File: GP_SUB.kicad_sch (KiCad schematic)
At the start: 35 parts, among them J13 Conn_01x10, J14 Conn_01x10, J32 Conn_01x02, J5 Conn_02x10_Odd_Even, U1 TPS76333, U2 TXB0104RUT, U5 TXB0104RUT

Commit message: Rails alim + libs
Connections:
- net SD_MOS renamed SDMOS
- net VBUS renamed P5VAN

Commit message: Ready for review
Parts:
- removed R13, R14, R15, R16, R17, R18, R19, R20: 0R, Resistor_SMD:R_0201_0603Metric, symbol Device:R_Small
- removed R40, R42, R43, R45, R46, R48, R49, R51: 0R, Resistor_SMD:R_0603_1608Metric, symbol Device:R_Small
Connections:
- net P11 is gone; now on net TP7_Pin11: J13.7 (Pin_7), J5.13 (Pin_13)
- net P12 is gone; now on net TP15_Pin12: J14.6 (Pin_6), J5.5 (Pin_5)
- net P13 is gone; now on net TP8_Pin13: J13.8 (Pin_8), J5.14 (Pin_14)
- net P14: now also U2.2 (A1)
- net P16: now also U2.3 (A2)
- net P7: now also U2.5 (A4)
- net P8: now also U5.5 (A4)
- net P9: now also U5.3 (A2)
- net TP15_Pin12: no longer U2.8 (B3)
- net TP7_Pin11: no longer U5.10 (B1)
- net TP8_Pin13: no longer U5.8 (B3)
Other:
- note removed: "Bypass LevelShifter"

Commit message: For review
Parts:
- R8: value 1k -> 4k7
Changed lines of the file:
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@@
 			)
 		)
-		(property "Value" "1k"
+		(property "Value" "4k7"
 			(at 139.319 37.973 0)
 			(show_name no)

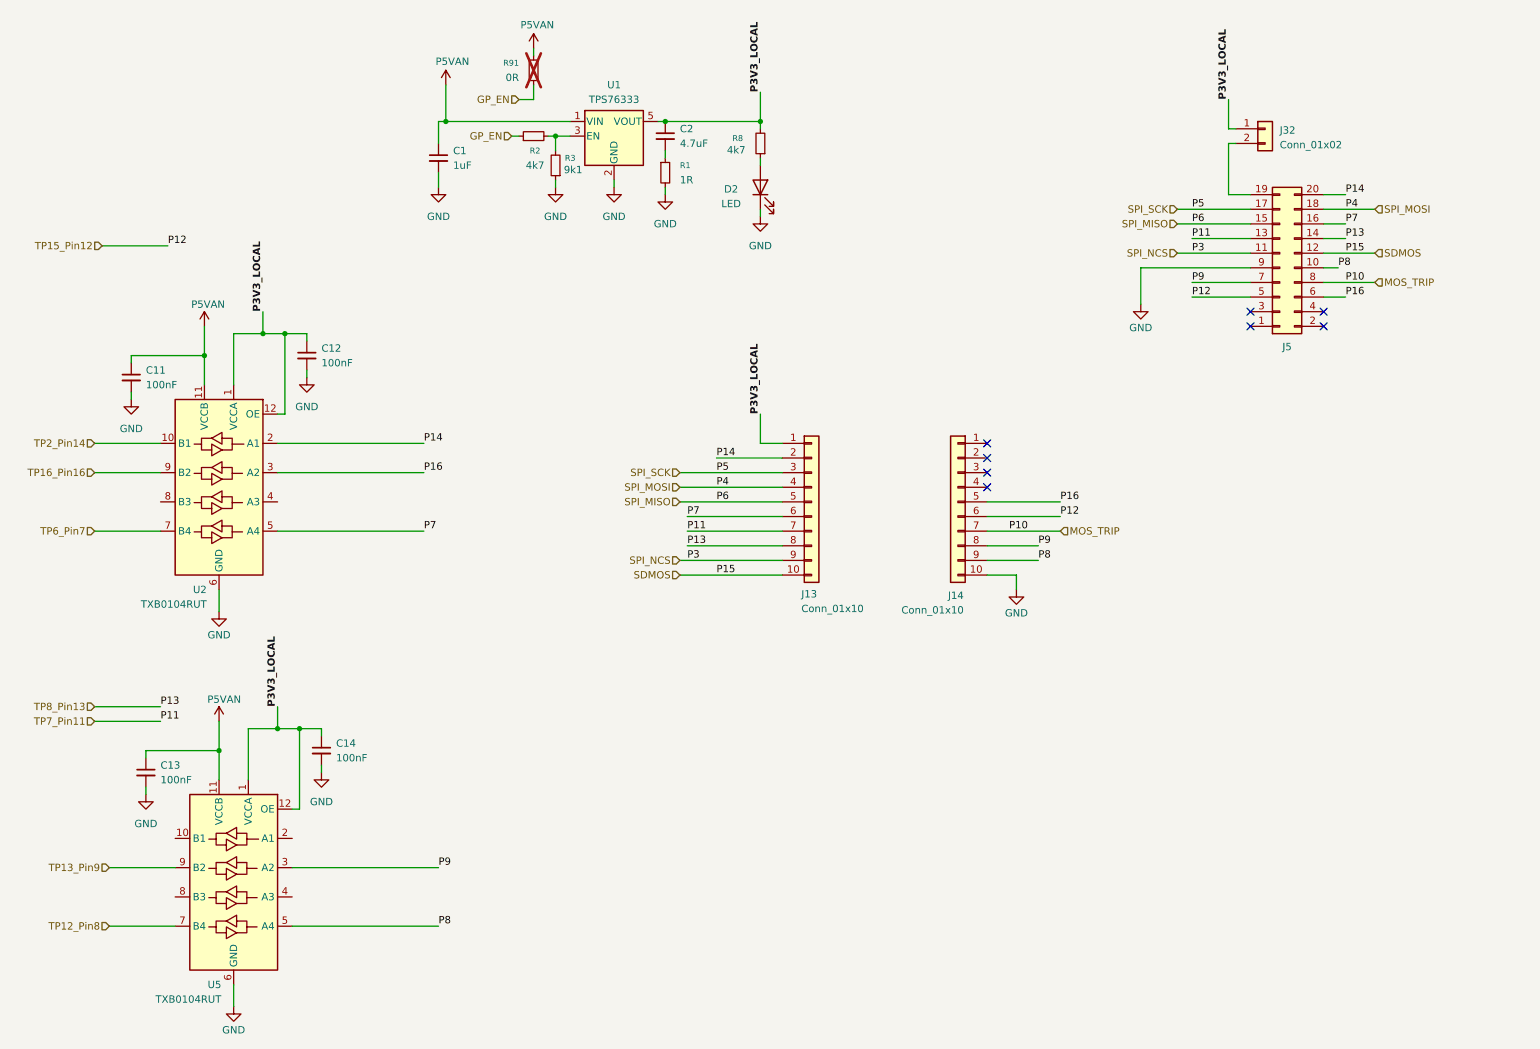
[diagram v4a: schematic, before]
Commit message: Refactor GreenPak Pinout
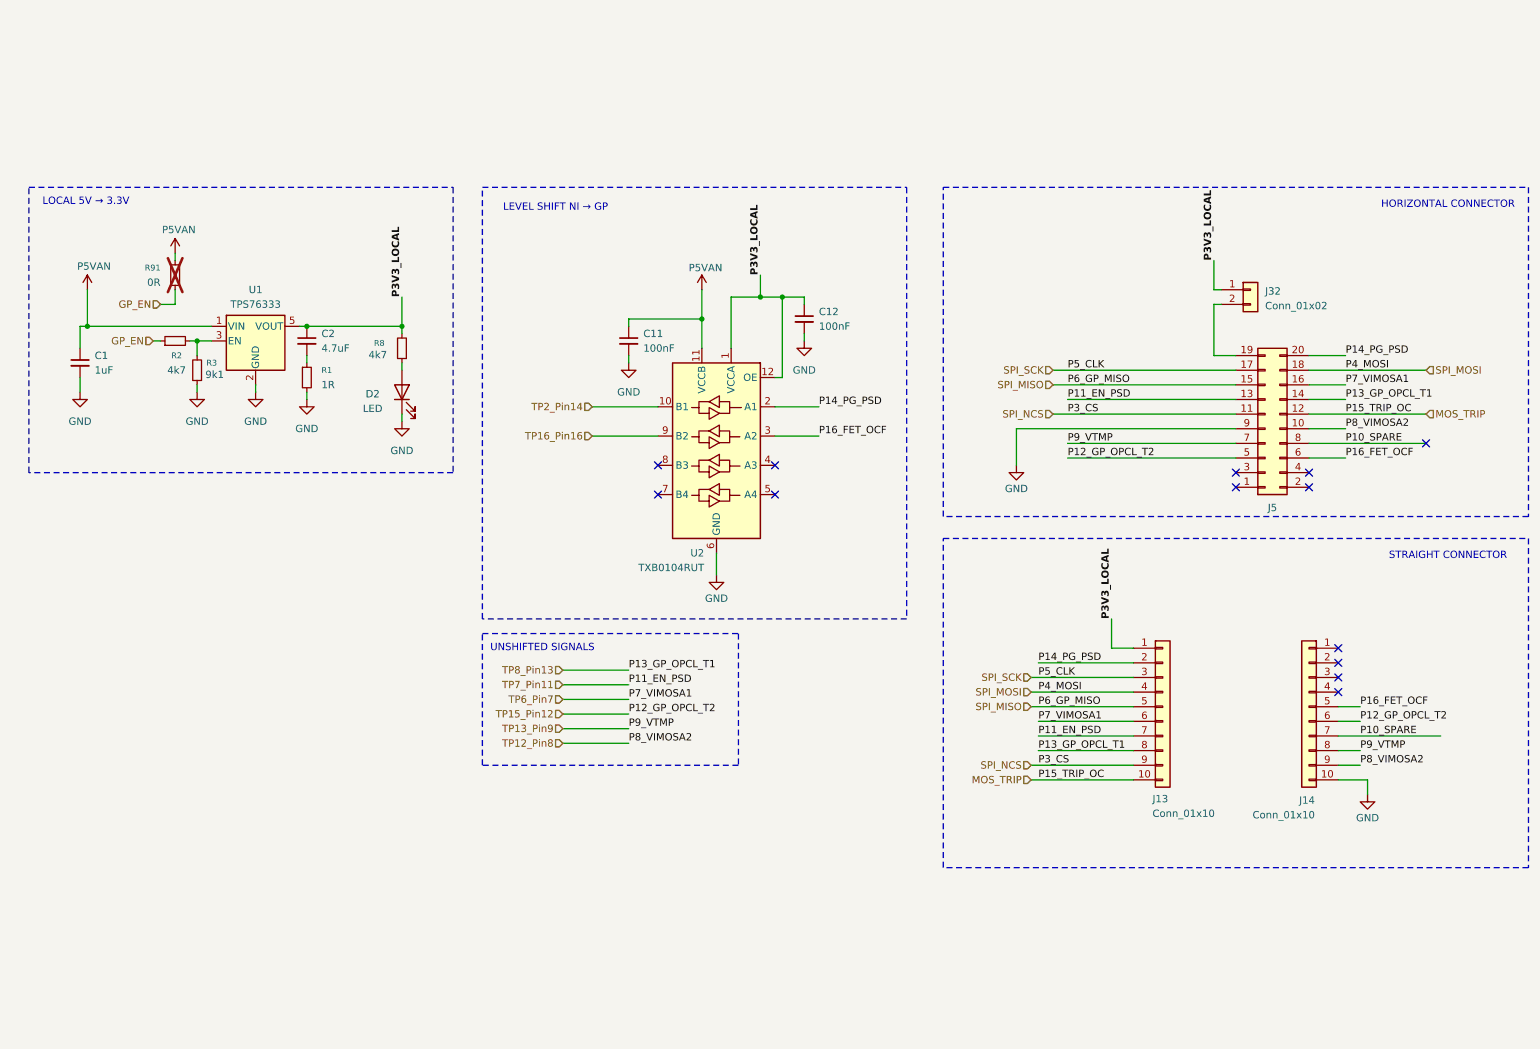
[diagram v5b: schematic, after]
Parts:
- removed C13, C14: 100nF, Capacitor_SMD:C_0402_1005Metric, symbol Device:C_Small
- removed U5: TXB0104RUT, Package_DFN_QFN:Texas_R-PUQFN-N12, symbol Logic_LevelTranslator:TXB0104RUT
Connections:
- net P8 is gone; now on net TP12_Pin8: J14.9 (Pin_9), J5.10 (Pin_10)
- net P9 is gone; now on net TP13_Pin9: J14.8 (Pin_8), J5.7 (Pin_7)
- net SDMOS is gone; now on net MOS_TRIP: J13.10 (Pin_10), J5.12 (Pin_12)
- net MOS_TRIP: no longer J14.7 (Pin_7), J5.8 (Pin_8)
- net TP6_Pin7: now also J13.6 (Pin_6), J5.16 (Pin_16); no longer U2.7 (B4)
- net P14 renamed P14_PG_PSD
- net P16 renamed P16_FET_OCF
- removed net P7: J13.6 (Pin_6), J5.16 (Pin_16), U2.5 (A4)
- new net P10_SPARE: J14.7 (Pin_7), J5.8 (Pin_8)
- no-connect marks 8 -> 13
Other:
- note added: "HORIZONTAL CONNECTOR"
- note added: "LEVEL SHIFT NI → GP"
- note added: "LOCAL 5V → 3.3V"
- note added: "STRAIGHT CONNECTOR"
- note added: "UNSHIFTED SIGNALS"
- moved on the sheet: C1, C11, C12, C2, D2, J13, J14, J32, J5, R1, R2, R3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

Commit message: OPCL via LevelShifters
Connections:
- net MOS_TRIP: now also U2.7 (B4); no longer J13.10 (Pin_10), J5.12 (Pin_12)
- net P15_TRIP_OC: now reaches U2.5 (A4)
- net P15_TRIP_OC: now also J13.10 (Pin_10), J5.12 (Pin_12)
- no-connect marks 13 -> 10
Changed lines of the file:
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@@
-	)
-	(no_connect
-		(at 259.08 88.9)
 	)
 	(no_connect
@@
 	)
 	(no_connect
+		(at 243.84 124.46)
+	)
+	(no_connect
+		(at 243.84 129.54)
+	)
+	(no_connect
+		(at 238.76 96.52)
+	)
+	(no_connect
 		(at 146.05 92.71)
 	)
 	(no_connect
-		(at 125.73 97.79)
+		(at 243.84 127)
 	)
 	(no_connect
-		(at 243.84 124.46)
+		(at 226.06 93.98)
+	)
+	(no_connect
+		(at 243.84 132.08)
 	)
 	(no_connect
 		(at 125.73 92.71)
 	)
-	(no_connect
-		(at 243.84 129.54)
-	)
-	(no_connect
-		(at 238.76 96.52)
-	)
-	(no_connect
-		(at 243.84 127)
-	)
-	(no_connect
-		(at 146.05 97.79)
-	)
-	(no_connect
-		(at 226.06 93.98)
-	)
-	(no_connect
-		(at 243.84 132.08)
-	)
 	(wire
 		(pts
@@
 	(wire
 		(pts
-			(xy 238.76 83.82) (xy 259.08 83.82)
+			(xy 238.76 83.82) (xy 245.11 83.82)
 		)
 		(stroke
@@
 	(wire
 		(pts
-			(xy 190.5 147.32) (xy 208.28 147.32)
-		)
-		(stroke
-			(width 0)
-			(type default)
-		)
-	)
-	(wire
-		(pts
 			(xy 64.77 68.58) (xy 81.28 68.58)
 		)
@@
 	(wire
 		(pts
+			(xy 114.3 97.79) (xy 125.73 97.79)
+		)
+		(stroke
+			(width 0)
+			(type default)
+		)
+	)
+	(wire
+		(pts
+			(xy 146.05 97.79) (xy 153.67 97.79)
+		)
+		(stroke
+			(width 0)
+			(type default)
+		)
+	)
+	(wire
+		(pts
 			(xy 190.5 129.54) (xy 208.28 129.54)
 		)
@@
 	(wire
 		(pts
-			(xy 243.84 139.7) (xy 261.62 139.7)
+			(xy 243.84 139.7) (xy 247.65 139.7)
 		)
 		(stroke
@@
 	(wire
 		(pts
+			(xy 191.77 147.32) (xy 208.28 147.32)
+		)
+		(stroke
+			(width 0)
+			(type default)
+		)
+	)
+	(wire
+		(pts
 			(xy 45.72 71.12) (xy 45.72 73.66)
 		)
@@
 	(wire
 		(pts
-			(xy 238.76 88.9) (xy 259.08 88.9)
+			(xy 238.76 88.9) (xy 245.11 88.9)
 		)
 		(stroke
@@
 		)
 	)
+	(label "P15_TRIP_OC"
+		(at 153.67 97.79 0)
+		(effects
+			(font
+				(size 1.27 1.27)
+			)
+			(justify left bottom)
+		)
+	)
 	(label "P7_VIMOSA1"
 		(at 120.65 133.35 0)
@@
 		)
 	)
-	(hierarchical_label "MOS_TRIP"
-		(shape input)
-		(at 259.08 83.82 0)
-		(effects
-			(font
-				(size 1.27 1.27)
-			)
-			(justify left)
-		)
-	)
 	(hierarchical_label "TP7_Pin11"
 		(shape input)
@@
 		)
 	)
-	(hierarchical_label "MOS_TRIP"
-		(shape input)
-		(at 190.5 147.32 180)
-		(effects
-			(font
-				(size 1.27 1.27)
-			)
-			(justify right)
-		)
-	)
 	(hierarchical_label "TP12_Pin8"
 		(shape input)
@@
 		(effects
 			(font
+				(size 1.27 1.27)
+			)
+			(justify right)
+		)
+	)
+	(hierarchical_label "MOS_TRIP"
+		(shape input)
+		(at 114.3 97.79 180)
+		(effects
+			(font
